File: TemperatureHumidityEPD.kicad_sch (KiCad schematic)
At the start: 53 parts, among them J1 Conn_01x08, J3 Conn_01x02, J4 Conn_01x24, J5 FTSH-105-01-L-DV-K, Q1 IRLML6344, Q2 Si1308EDL, U2 SI7021, U3 MAX32660GTP, Y1 32.7680KHZ

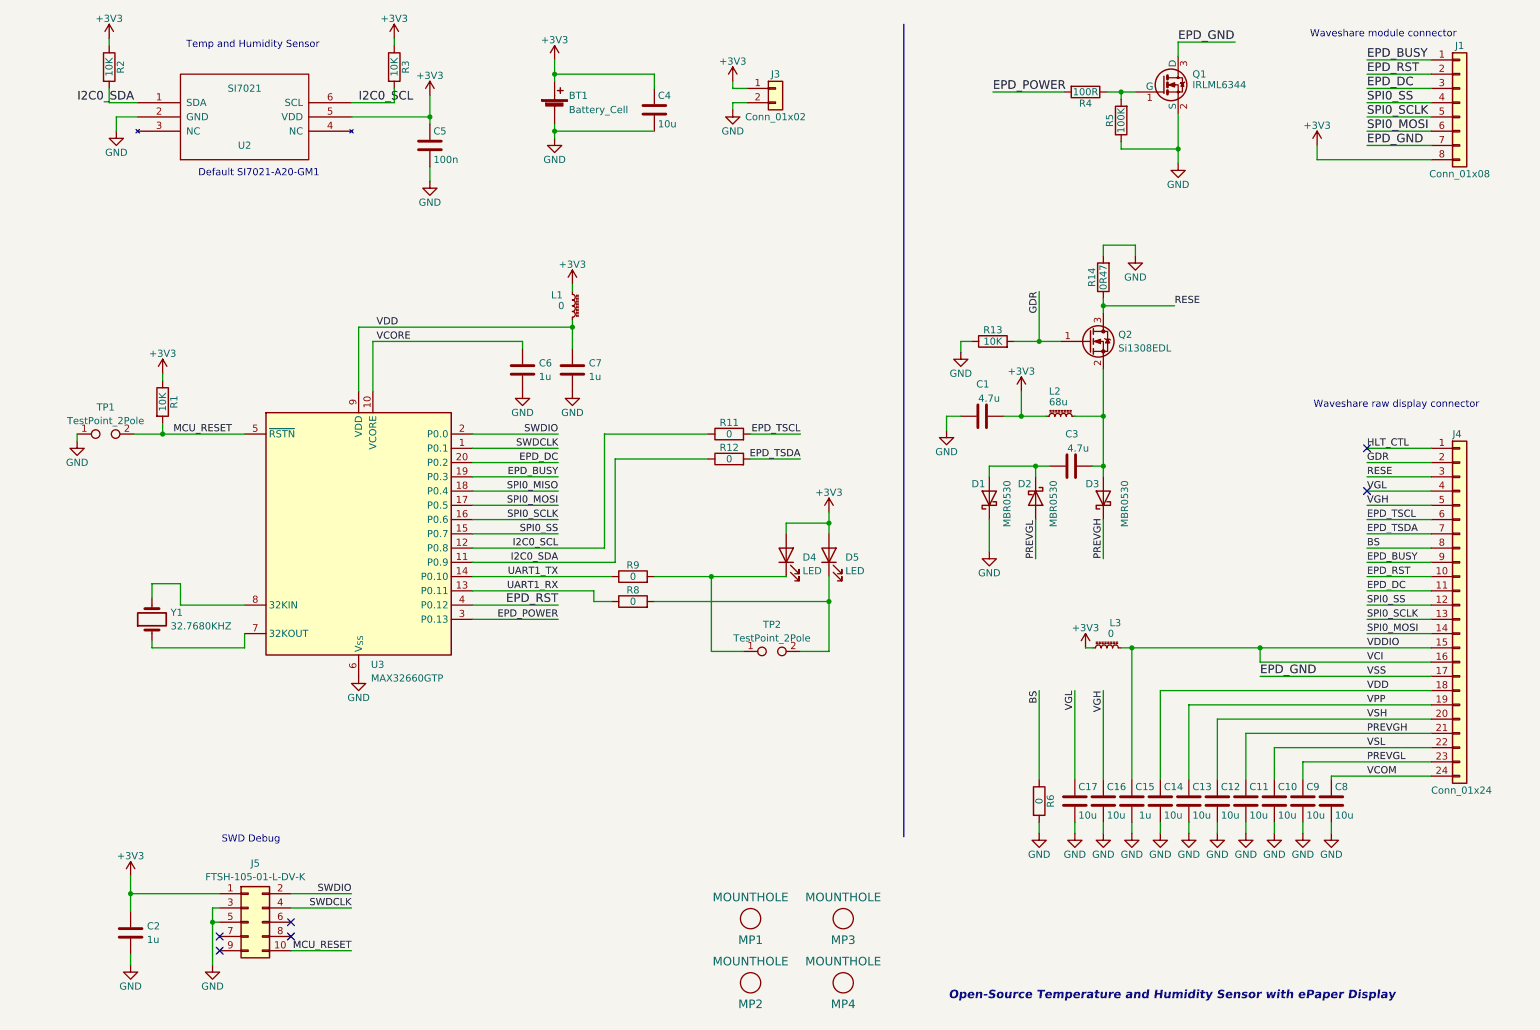
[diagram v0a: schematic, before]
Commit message: Added buck-boost for constant 3.3Vout.
Fixes for ePaper display power.

Double-check part availability.

Final footprint reference changes in schematic.
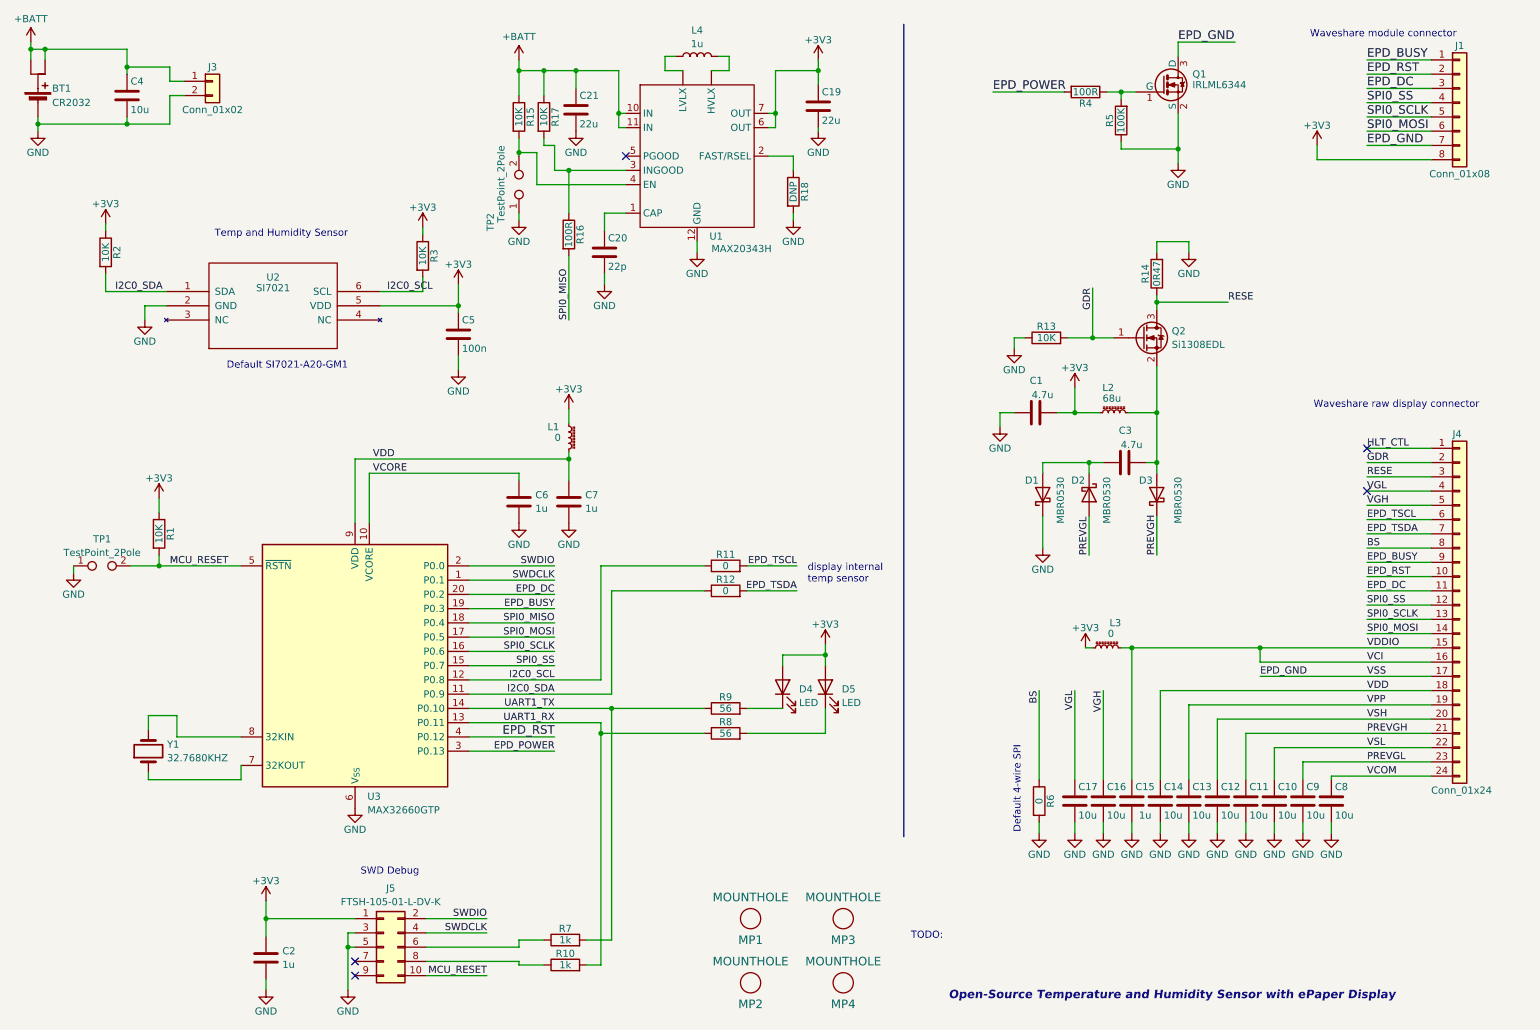
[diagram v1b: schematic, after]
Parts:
- added C19, C21: 22u, Capacitor_SMD:C_1206_3216Metric_Pad1.33x1.80mm_HandSolder, symbol TemperatureHumidityEPD-rescue:C
- added C20: 22p, Capacitor_SMD:C_0603_1608Metric_Pad1.08x0.95mm_HandSolder, symbol TemperatureHumidityEPD-rescue:C
- added L4: 1u, Inductors_Custom:L_0805_2016Metric, symbol Device:L
- added R10, R7: 1k, Resistor_SMD:R_0603_1608Metric_Pad0.98x0.95mm_HandSolder, symbol TemperatureHumidityEPD-rescue:R
- added R15, R17: 10K, Resistor_SMD:R_0603_1608Metric_Pad0.98x0.95mm_HandSolder, symbol TemperatureHumidityEPD-rescue:R
- added R16: 100R, Resistor_SMD:R_0603_1608Metric_Pad0.98x0.95mm_HandSolder, symbol TemperatureHumidityEPD-rescue:R
- added R18: DNP, Resistor_SMD:R_0603_1608Metric_Pad0.98x0.95mm_HandSolder, symbol TemperatureHumidityEPD-rescue:R
- added U1: MAX20343H, ADI_Power:MAX20343H, symbol ADI_Power:MAX20343H
- BT1: value Battery_Cell -> CR2032; footprint (none) -> Connectors_Custom:BatteryHolder_TE_BATT-HLD-000_1x2032; symbol TemperatureHumidityEPD-rescue:Battery_Cell -> Connectors_Custom:Battery_Cell_Holder
- J5: footprint (none) -> Connectors_Custom:SAMTEC_FTSH-105-01-L-DV-K
- L2: footprint (none) -> Inductors_Custom:L_3x3_H3
- R8, R9: value 0 -> 56; Part Number RCS06030000Z0EC -> RC0603FR-0756RL
- TP1, TP2: footprint TestPoint:TestPoint_Bridge_Pitch2.0mm_Drill0.7mm -> TestPoint:TestPoint_Bridge_Pitch2.54mm_Drill1.0mm
- U2: footprint KevinLibrary:SI7021 -> Silabs_custom:SI7021
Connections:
- net +3V3: now also C19.1, U1.6 (OUT), U1.7 (OUT); no longer BT1.1 (+), C4.1, J3.1 (Pin_1)
- net GND: now also BT1.3 (-), TP2.1, C19.2, C20.2, C21.2, R18.2, U1.12 (GND); no longer BT1.2 (-)
- net SPI0_MISO: now also R16.2
- net UART1_RX: now also R10.2
- net UART1_TX: now also R7.2
- net at D5.1 (K), R8.2: no longer TP2.2
- net at J5.6 (Pin_6): now also R7.1
- net at J5.8 (Pin_8): now also R10.1
- net at D4.1 (K), R9.2: no longer TP2.1
- new net: R16.1, R17.2, U1.3 (INGOOD)
- new net: L4.1, U1. (LVLX)
- new net: L4.2, U1. (LVLX)
- new net: C20.1, U1.1 (CAP)
- new net: R15.2, TP2.2, U1.4 (EN)
- new net: R18.1, U1.2 (FAST/RSEL)
- new net +BATT: BT1.1 (+), BT1.2 (+), C21.1, C4.1, J3.1 (Pin_1), R15.1, R17.1, U1.10 (IN), U1.11 (IN)
- no-connect marks 6 -> 5
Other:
- note added: "Default 4-wire SPI"
- note added: "TODO:"
- note added: "display internal temp sensor"
- moved on the sheet: C1, C2, C3, C4, C5, C6, C7, D1, D2, D3, D4, D5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

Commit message: Completely finished layout. Various small schematic tweaks along the way of layout.
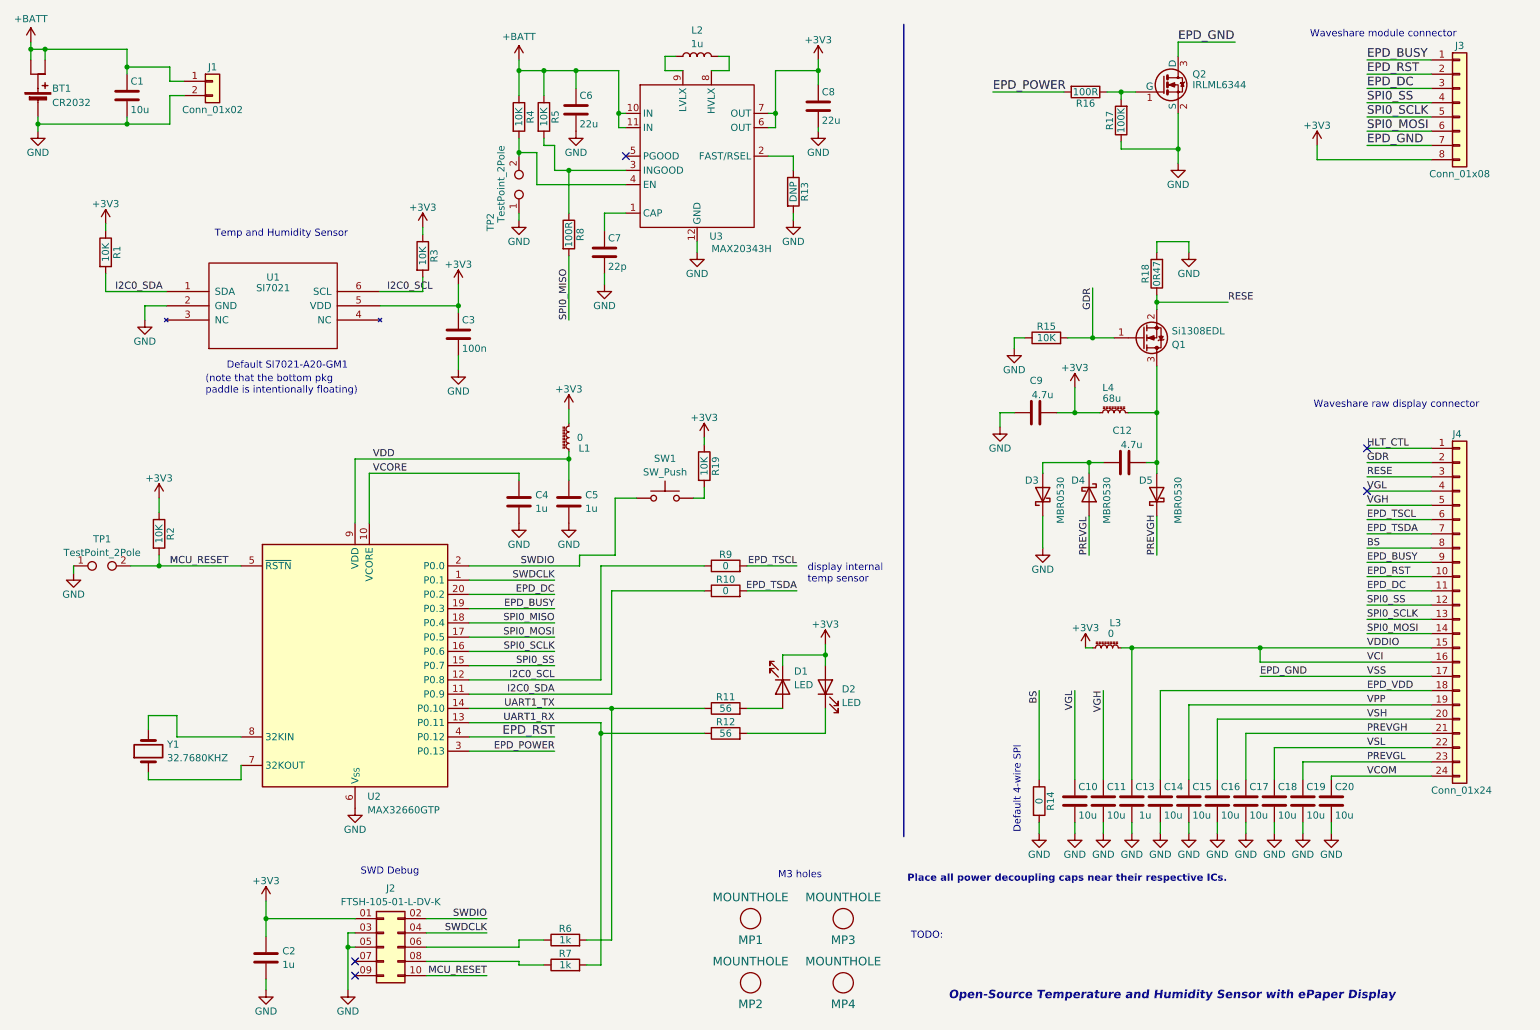
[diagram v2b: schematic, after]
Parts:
- added R19: 10K, Resistor_SMD:R_0603_1608Metric_Pad0.98x0.95mm_HandSolder, symbol TemperatureHumidityEPD-rescue:R
- added SW1: SW_Push, Switch_Custom:Panasonic_EVQPUJ_EVQPUA, symbol Switch:SW_Push
- C12: renamed from C3; footprint Capacitors_SMD:C_0805_HandSoldering -> Capacitor_SMD:C_0805_2012Metric_Pad1.18x1.45mm_HandSolder
- C9: renamed from C1; footprint Capacitors_SMD:C_0805_HandSoldering -> Capacitor_SMD:C_0805_2012Metric_Pad1.18x1.45mm_HandSolder
- J1: renamed from J3; footprint Pin_Headers:Pin_Header_Straight_1x02_Pitch2.54mm -> Connectors_Custom:Pin_Header_Straight_1x02_Pitch2.54mm
- J3: renamed from J1; footprint Pin_Headers:Pin_Header_Straight_1x08_Pitch2.54mm -> Connector_JST:JST_PH_S8B-PH-SM4-TB_1x08-1MP_P2.00mm_Horizontal
- J4: footprint Connector_FFC-FPC:TE_2-1734839-4_1x24-1MP_P0.5mm_Horizontal -> Connectors_Custom:TE_2-1734839-4_1x24-1MP_P0.5mm_Horizontal_reversednumber
- MP1, MP2, MP3, MP4: footprint KevinLibrary:TH-M3 -> Connectors_Custom:TH-M3
- Q2: renamed from Q1; footprint TO_SOT_Packages_SMD:SOT-23 -> Package_TO_SOT_SMD:SOT-23-3
- TP1, TP2: footprint TestPoint:TestPoint_Bridge_Pitch2.54mm_Drill1.0mm -> Connectors_Custom:TestPoint_Padx2_D2.0mm
- renumbered C4 to C1, C17 to C10, C16 to C11, C15 to C13, C13 to C15, C12 to C16, C11 to C17, C10 to C18, C9 to C19, C8 to C20, C5 to C3, C6 to C4, C7 to C5, C21 to C6, C20 to C7, C19 to C8, D4 to D1, D5 to D2, D1 to D3, D2 to D4, D3 to D5, J5 to J2, L4 to L2, L2 to L4, Q2 to Q1, R2 to R1, R12 to R10, R9 to R11, R8 to R12, R18 to R13, R6 to R14, R13 to R15, R4 to R16, R5 to R17, R14 to R18, R1 to R2, R15 to R4, R17 to R5, R7 to R6, R10 to R7, R16 to R8, R11 to R9, U2 to U1, U3 to U2, U1 to U3
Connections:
- net +3V3: now also D1.1 (K), J2.01 (Pin_1), L1.2, R19.1; no longer D1.2 (A), J2.1 (Pin_1), L1.1
- net GND: now also J2.03 (Pin_3), J2.05 (Pin_5); no longer J2.3 (Pin_3), J2.5 (Pin_5)
- net RESE: now also Q1.2 (S); no longer Q1.3 (D)
- net SWDCLK: now also J2.04 (Pin_4); no longer J2.4 (Pin_4)
- net SWDIO: now also J2.02 (Pin_2), SW1.1; no longer J2.2 (Pin_2)
- net VDD: now also L1.1; no longer C14.1, J4.18 (Pin_18), L1.2
- net at L2.1: now also U3.9 (LVLX); no longer U3. (LVLX)
- net at L2.2: now also U3.8 (HVLX); no longer U3. (LVLX)
- net at C12.2, D5.2 (A), L4.2: now also Q1.3 (D); no longer Q1.2 (S)
- net at R6.1: now also J2.06 (Pin_6); no longer J2.6 (Pin_6)
- net at R7.1: now also J2.08 (Pin_8); no longer J2.8 (Pin_8)
- net at R11.2: now also D1.2 (A); no longer D1.1 (K)
- new net: R19.2, SW1.2
- new net EPD_VDD: C14.1, J4.18 (Pin_18)
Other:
- note added: "(note that the bottom pkg paddle is intentionally floating)"
- note added: "M3 holes"
- note added: "Place all power decoupling caps near their respective ICs."
- moved on the sheet: D1, L1
